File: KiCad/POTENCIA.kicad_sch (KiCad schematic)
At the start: 23 parts, among them J5 Screw_Terminal_01x04, M4 Motor_DC, M5 Motor_DC, M6 Motor_DC, Q2 IRLZ44N, U5 TB6612FNG, U7 ATtiny1616-M, U8 DRV8871DDA

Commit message: cambios en organizacion
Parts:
- removed R27: 10k, Resistor_SMD:R_0805_2012Metric, symbol Device:R
- removed R28, R29: 3.6, Resistor_SMD:R_0805_2012Metric, symbol Device:R
- added R1: 10k, Resistor_SMD:R_0805_2012Metric, symbol Device:R
- added R2, R3: 3.6, Resistor_SMD:R_0805_2012Metric, symbol Device:R
- renumbered C31 to C?, C9 to C?, C33 to C?, C30 to C?, C32 to C?, C34 to C?, D5 to D?, J5 to J?, M5 to M?, M4 to M?, M6 to M?, Q2 to Q?, R24 to R?, R23 to R?, R14 to R?, R1 to R?, R26 to R?, U5 to U?, U7 to U?, U8 to U?
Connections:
- net +3.3V: now also R2.2
- net CALEFACCIÓ: now also R1.1, R3.1
- net GND: now also R1.2
- net T_SEIENTS: now also R2.1
- net at D?.2 (A): now also R3.2
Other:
- moved on the sheet: D?, J?, Q?

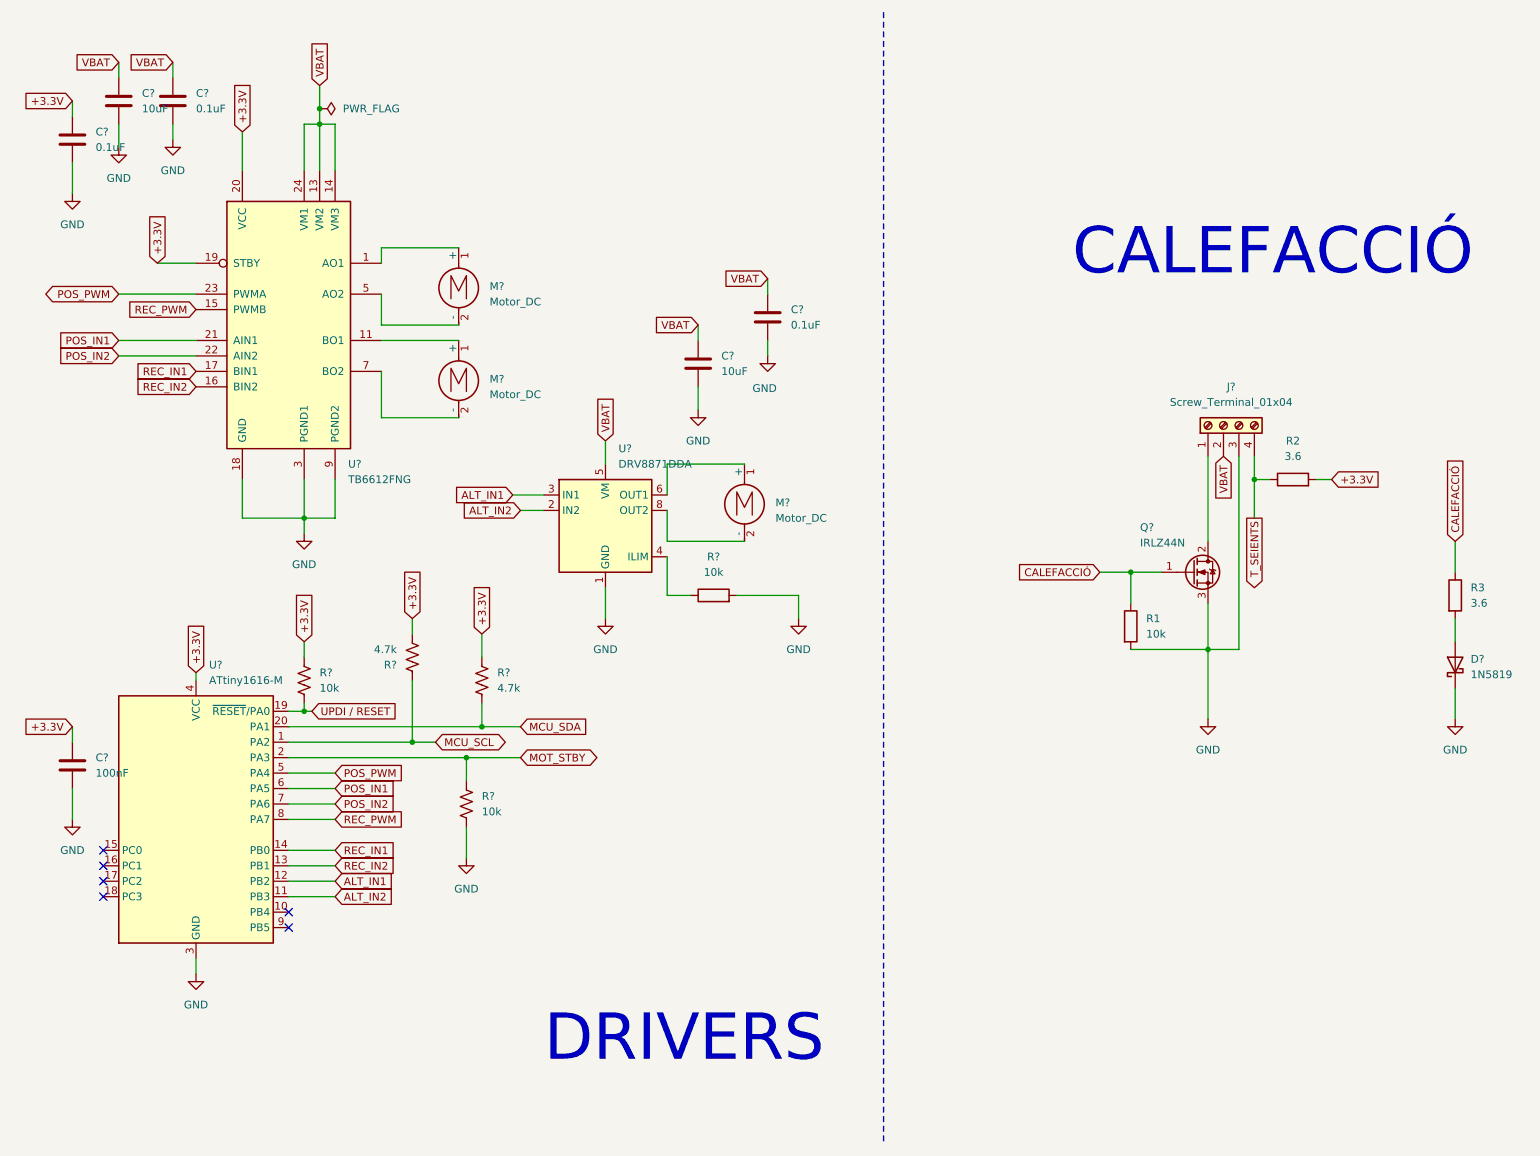
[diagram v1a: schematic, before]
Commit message: Modificació d'errors varis
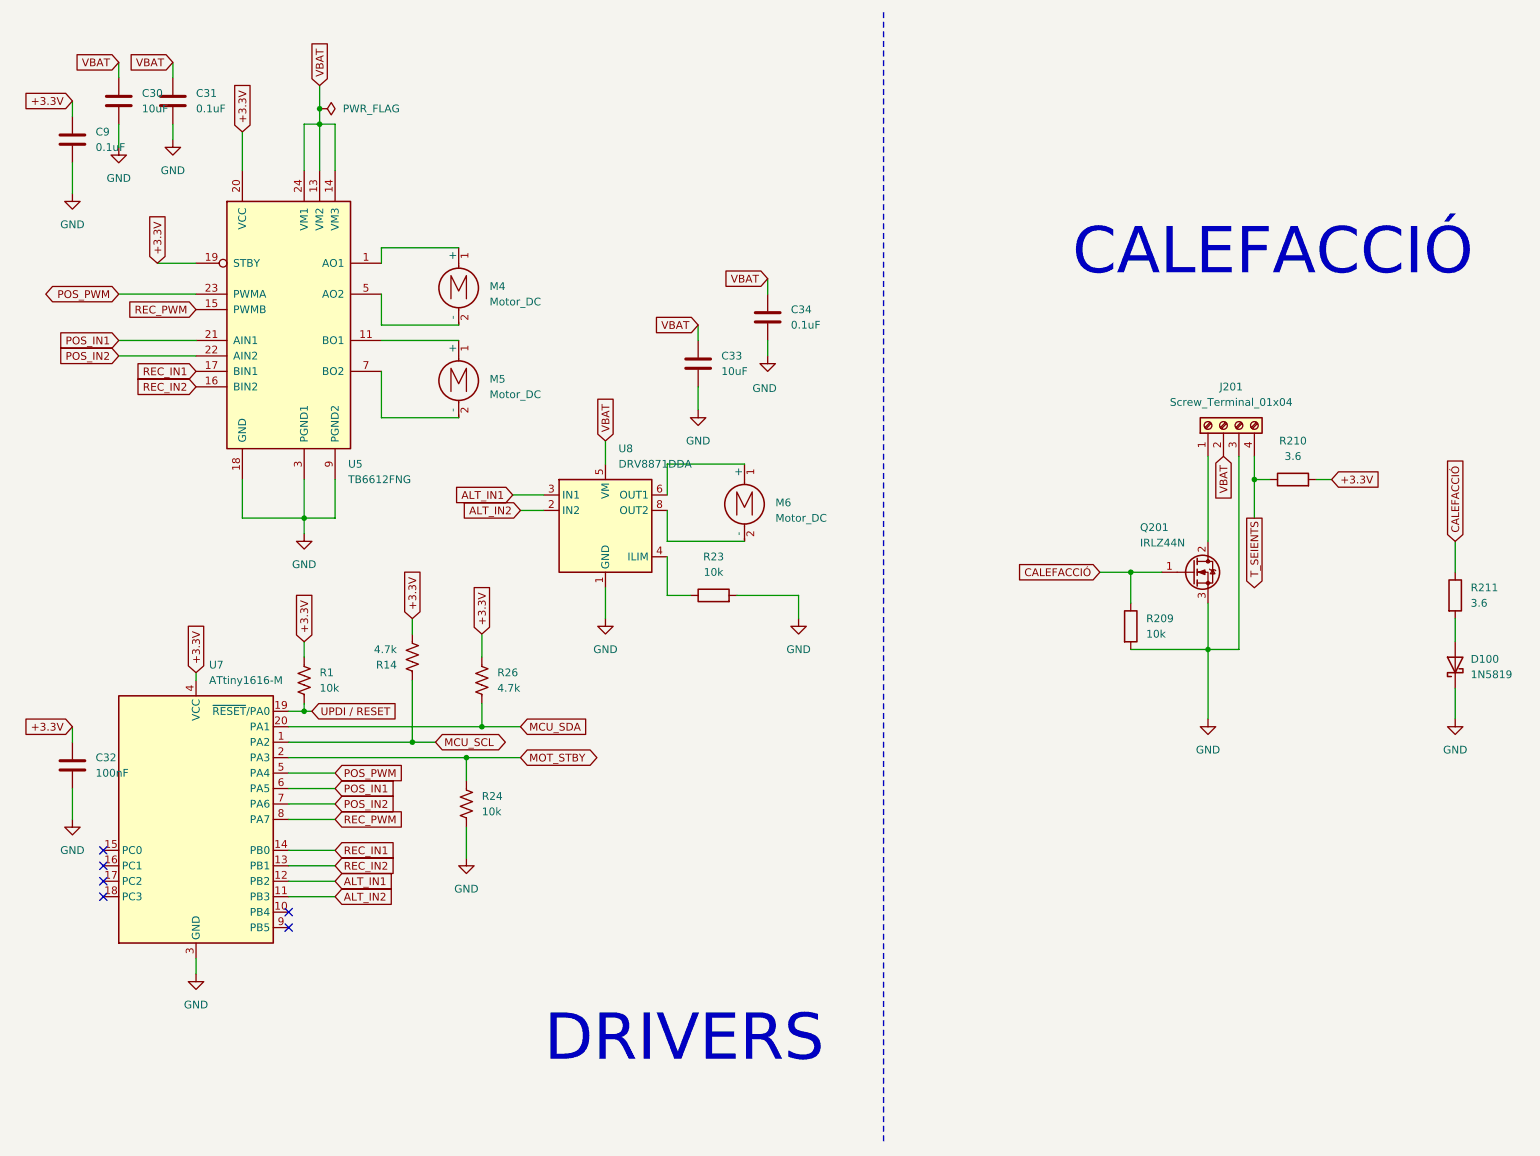
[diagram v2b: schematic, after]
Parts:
- gave numbers to parts that had none: 20
- renumbered R1 to R209, R2 to R210, R3 to R211
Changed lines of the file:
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@@
 	(wire
 		(pts
-			(xy 213.36 85.09) (xy 213.36 99.06)
-		)
-		(stroke
-			(width 0)
-			(type default)
-		)
-	)
-	(wire
-		(pts
 			(xy 40.64 53.34) (xy 46.99 53.34)
 		)
@@
 	(wire
 		(pts
+			(xy 213.36 85.09) (xy 213.36 99.06)
+		)
+		(stroke
+			(width 0)
+			(type default)
+		)
+	)
+	(wire
+		(pts
 			(xy 62.23 134.62) (xy 91.44 134.62)
 		)
@@
 		(dnp no)
 		(fields_autoplaced yes)
-		(property "Reference" "#PWR?"
+		(property "Reference" "#PWR052"
 			(at 129.54 83.82 0)
 			(effects
@@
 		(dnp no)
 		(fields_autoplaced yes)
-		(property "Reference" "R?"
+		(property "Reference" "R24"
 			(at 93.98 140.9699 0)
 			(effects
@@
 		(dnp no)
 		(fields_autoplaced yes)
-		(property "Reference" "#PWR?"
+		(property "Reference" "#PWR048"
 			(at 64.77 104.14 0)
 			(effects
@@
 		(dnp no)
 		(fields_autoplaced yes)
-		(property "Reference" "R?"
+		(property "Reference" "R23"
 			(at 132.08 101.6 90)
 			(effects
@@
 		(on_board yes)
 		(dnp no)
-		(property "Reference" "Q?"
+		(property "Reference" "Q201"
 			(at 202.184 96.774 0)
 			(effects
@@
 				)
 			)
+			(project "SEIENTS_EDD"
+				(path "/b6401b4f-5426-49b8-bb2e-8ecdb19989ef/59990b35-698c-4572-9d1a-e1ee1d49a527"
+					(reference "Q201")
+					(unit 1)
+				)
+			)
 		)
 	)
@@
 		(dnp no)
 		(fields_autoplaced yes)
-		(property "Reference" "U?"
+		(property "Reference" "U5"
 			(at 71.9933 86.36 0)
 			(effects
@@
 		(dnp no)
 		(fields_autoplaced yes)
-		(property "Reference" "#PWR?"
+		(property "Reference" "#PWR055"
 			(at 146.05 118.11 0)
 			(effects
@@
 		(dnp no)
 		(fields_autoplaced yes)
-		(property "Reference" "#PWR02"
+		(property "Reference" "#PWR0106"
 			(at 254 134.62 0)
 			(effects
@@
 				)
 			)
+			(project "SEIENTS_EDD"
+				(path "/b6401b4f-5426-49b8-bb2e-8ecdb19989ef/59990b35-698c-4572-9d1a-e1ee1d49a527"
+					(reference "#PWR0106")
+					(unit 1)
+				)
+			)
 		)
 	)
@@
 		(dnp no)
 		(fields_autoplaced yes)
-		(property "Reference" "U?"
+		(property "Reference" "U7"
 			(at 49.1333 119.38 0)
 			(effects
@@
 		(dnp no)
 		(fields_autoplaced yes)
-		(property "Reference" "C?"
+		(property "Reference" "C31"
 			(at 46.99 25.3999 0)
 			(effects
@@
 		(dnp no)
 		(fields_autoplaced yes)
-		(property "Reference" "#PWR?"
+		(property "Reference" "#PWR053"
 			(at 91.44 157.48 0)
 			(effects
@@
 		(dnp no)
 		(fields_autoplaced yes)
-		(property "Reference" "C?"
+		(property "Reference" "C9"
 			(at 30.48 31.7499 0)
 			(effects
@@
 		(dnp no)
 		(fields_autoplaced yes)
-		(property "Reference" "M?"
+		(property "Reference" "M5"
 			(at 95.25 72.3899 0)
 			(effects
@@
 		(dnp no)
 		(fields_autoplaced yes)
-		(property "Reference" "C?"
+		(property "Reference" "C33"
 			(at 133.35 68.5799 0)
 			(effects
@@
 		(dnp no)
 		(fields_autoplaced yes)
-		(property "Reference" "#PWR?"
+		(property "Reference" "#PWR049"
 			(at 26.67 151.13 0)
 			(effects
@@
 		(dnp no)
 		(fields_autoplaced yes)
-		(property "Reference" "C?"
+		(property "Reference" "C30"
 			(at 38.1 25.3999 0)
 			(effects
@@
 		(dnp no)
 		(fields_autoplaced yes)
-		(property "Reference" "#PWR?"
+		(property "Reference" "#PWR017"
 			(at 26.67 48.26 0)
 			(effects
@@
 		(dnp no)
 		(fields_autoplaced yes)
-		(property "Reference" "#PWR?"
+		(property "Reference" "#PWR020"
 			(at 34.29 40.64 0)
 			(effects
@@
 		(dnp no)
 		(fields_autoplaced yes)
-		(property "Reference" "#FLG?"
+		(property "Reference" "#FLG05"
 			(at 69.215 27.94 0)
 			(effects
@@
 		(on_board yes)
 		(dnp no)
-		(property "Reference" "M?"
+		(property "Reference" "M4"
 			(at 95.25 57.1499 0)
 			(effects
@@
 		(dnp no)
 		(fields_autoplaced yes)
-		(property "Reference" "#PWR01"
+		(property "Reference" "#PWR0102"
 			(at 213.36 134.62 0)
 			(effects
@@
 				)
 			)
+			(project "SEIENTS_EDD"
+				(path "/b6401b4f-5426-49b8-bb2e-8ecdb19989ef/59990b35-698c-4572-9d1a-e1ee1d49a527"
+					(reference "#PWR0102")
+					(unit 1)
+				)
+			)
 		)
 	)
@@
 		(dnp no)
 		(fields_autoplaced yes)
-		(property "Reference" "D?"
+		(property "Reference" "D100"
 			(at 256.54 118.4274 90)
 			(effects
@@
 				)
 			)
+			(project "SEIENTS_EDD"
+				(path "/b6401b4f-5426-49b8-bb2e-8ecdb19989ef/59990b35-698c-4572-9d1a-e1ee1d49a527"
+					(reference "D100")
+					(unit 1)
+				)
+			)
 		)
 	)
@@
 		(dnp no)
 		(fields_autoplaced yes)
-		(property "Reference" "R3"
+		(property "Reference" "R211"
 			(at 256.54 106.6799 0)
 			(effects
@@
 				)
 			)
+			(project "SEIENTS_EDD"
+				(path "/b6401b4f-5426-49b8-bb2e-8ecdb19989ef/59990b35-698c-4572-9d1a-e1ee1d49a527"
+					(reference "R211")
+					(unit 1)
+				)
+			)
 		)
 	)
@@
 		(on_board yes)
 		(dnp no)
-		(property "Reference" "#PWR?"
+		(property "Reference" "#PWR054"
 			(at 140.97 74.93 0)
 			(effects
@@
 		(dnp no)
 		(fields_autoplaced yes)
-		(property "Reference" "J?"
+		(property "Reference" "J201"
 			(at 217.17 73.66 90)
 			(effects
@@
 				)
 			)
+			(project "SEIENTS_EDD"
+				(path "/b6401b4f-5426-49b8-bb2e-8ecdb19989ef/59990b35-698c-4572-9d1a-e1ee1d49a527"
+					(reference "J201")
+					(unit 1)
+				)
+			)
 		)
 	)
@@
 		(dnp no)
 		(fields_autoplaced yes)
-		(property "Reference" "R1"
+		(property "Reference" "R209"
 			(at 203.2 111.7599 0)
 			(effects
@@
 				)
 			)
+			(project "SEIENTS_EDD"
+				(path "/b6401b4f-5426-49b8-bb2e-8ecdb19989ef/59990b35-698c-4572-9d1a-e1ee1d49a527"
+					(reference "R209")
+					(unit 1)
+				)
+			)
 		)
 	)
@@
 		(dnp no)
 		(fields_autoplaced yes)
-		(property "Reference" "U?"
+		(property "Reference" "U8"
 			(at 116.4433 83.82 0)
 			(effects
@@
 		(dnp no)
 		(fields_autoplaced yes)
-		(property "Reference" "C?"
+		(property "Reference" "C32"
 			(at 30.48 134.6199 0)
 			(effects
@@
 		(dnp no)
 		(fields_autoplaced yes)
-		(property "Reference" "#PWR?"
+		(property "Reference" "#PWR050"
 			(at 46.99 176.53 0)
 			(effects
@@
 		(dnp no)
 		(fields_autoplaced yes)
-		(property "Reference" "R?"
+		(property "Reference" "R14"
 			(at 80.01 119.3801 0)
 			(effects
@@
 		(dnp no)
 		(fields_autoplaced yes)
-		(property "Reference" "R?"
+		(property "Reference" "R1"
 			(at 67.31 120.6499 0)
 			(effects
@@
 		(dnp no)
 		(fields_autoplaced yes)
-		(property "Reference" "R?"
+		(property "Reference" "R26"
 			(at 96.52 120.6499 0)
 			(effects
@@
 		(dnp no)
 		(fields_autoplaced yes)
-		(property "Reference" "M?"
+		(property "Reference" "M6"
 			(at 142.24 92.7099 0)
 			(effects
@@
 		(dnp no)
 		(fields_autoplaced yes)
-		(property "Reference" "C?"
+		(property "Reference" "C34"
 			(at 144.78 60.9599 0)
 			(effects
@@
 		(dnp no)
 		(fields_autoplaced yes)
-		(property "Reference" "#PWR?"
+		(property "Reference" "#PWR026"
 			(at 43.18 39.37 0)
 			(effects
@@
 		(dnp no)
 		(fields_autoplaced yes)
-		(property "Reference" "#PWR?"
+		(property "Reference" "#PWR051"
 			(at 114.3 118.11 0)
 			(effects
@@
 		(dnp no)
 		(fields_autoplaced yes)
-		(property "Reference" "R2"
+		(property "Reference" "R210"
 			(at 227.33 82.55 90)
 			(effects
@@
 					(unit 1)
 				)
+			)
+			(project "SEIENTS_EDD"
+				(path "/b6401b4f-5426-49b8-bb2e-8ecdb19989ef/59990b35-698c-4572-9d1a-e1ee1d49a527"
+					(reference "R210")
+					(unit 1)
+				)

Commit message: FootPrints Canviats
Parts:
- M4, M5, M6: footprint Connector_PinHeader_2.54mm:PinHeader_1x02_P2.54mm_Horizontal -> TerminalBlock_Phoenix:TerminalBlock_Phoenix_MKDS-1,5-2-5.08_1x02_P5.08mm_Horizontal
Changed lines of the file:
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@@
 			)
 		)
-		(property "Footprint" "Connector_PinHeader_2.54mm:PinHeader_1x02_P2.54mm_Horizontal"
+		(property "Footprint" "TerminalBlock_Phoenix:TerminalBlock_Phoenix_MKDS-1,5-2-5.08_1x02_P5.08mm_Horizontal"
 			(at 90.17 73.406 0)
 			(effects
@@
 			)
 		)
-		(property "Footprint" "Connector_PinHeader_2.54mm:PinHeader_1x02_P2.54mm_Horizontal"
+		(property "Footprint" "TerminalBlock_Phoenix:TerminalBlock_Phoenix_MKDS-1,5-2-5.08_1x02_P5.08mm_Horizontal"
 			(at 90.17 58.166 0)
 			(effects
@@
 			)
 		)
-		(property "Footprint" "Connector_PinHeader_2.54mm:PinHeader_1x02_P2.54mm_Horizontal"
+		(property "Footprint" "TerminalBlock_Phoenix:TerminalBlock_Phoenix_MKDS-1,5-2-5.08_1x02_P5.08mm_Horizontal"
 			(at 137.16 93.726 0)
 			(effects

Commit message: Rounting
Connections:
- net ALT_IN1: now also U7.16 (PC1); no longer U7.12 (PB2)
- net ALT_IN2: now also U7.15 (PC0); no longer U7.11 (PB3)
- net REC_IN1: now also U7.13 (PB1); no longer U7.14 (PB0)
- net REC_IN2: now also U7.14 (PB0); no longer U7.13 (PB1)
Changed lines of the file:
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@@
 	)
 	(no_connect
-		(at 31.75 152.4)
+		(at 62.23 154.94)
 	)
 	(no_connect
@@
 	)
 	(no_connect
-		(at 31.75 149.86)
-	)
-	(wire
-		(pts
-			(xy 26.67 139.7) (xy 26.67 144.78)
+		(at 62.23 157.48)
+	)
+	(wire
+		(pts
+			(xy 26.67 139.7) (xy 26.67 140.97)
 		)
 		(stroke
@@
 	(wire
 		(pts
-			(xy 62.23 157.48) (xy 69.85 157.48)
-		)
-		(stroke
-			(width 0)
-			(type default)
-		)
-	)
-	(wire
-		(pts
 			(xy 93.98 125.73) (xy 93.98 129.54)
 		)
@@
 		(pts
 			(xy 54.61 88.9) (xy 54.61 95.25)
-		)
-		(stroke
-			(width 0)
-			(type default)
-		)
-	)
-	(wire
-		(pts
-			(xy 62.23 154.94) (xy 69.85 154.94)
 		)
 		(stroke
@@
 	(global_label "REC_IN1"
 		(shape input)
-		(at 69.85 149.86 0)
+		(at 69.85 152.4 0)
 		(fields_autoplaced yes)
 		(effects
@@
 		)
 		(property "Intersheetrefs" "${INTERSHEET_REFS}"
-			(at 80.6366 149.86 0)
+			(at 80.6366 152.4 0)
 			(effects
 				(font
@@
 	(global_label "ALT_IN2"
 		(shape input)
-		(at 69.85 157.48 0)
+		(at 31.75 149.86 180)
+		(fields_autoplaced yes)
+		(effects
+			(font
+				(size 1.27 1.27)
+			)
+			(justify right)
+		)
+		(property "Intersheetrefs" "${INTERSHEET_REFS}"
+			(at 22.2223 149.86 0)
+			(effects
+				(font
+					(size 1.27 1.27)
+				)
+				(justify right)
+				(hide yes)
+			)
+		)
+	)
+	(global_label "VBAT"
+		(shape input)
+		(at 34.29 20.32 180)
+		(fields_autoplaced yes)
+		(effects
+			(font
+				(size 1.27 1.27)
+			)
+			(justify right)
+		)
+		(property "Intersheetrefs" "${INTERSHEET_REFS}"
+			(at 27.5442 20.32 0)
+			(effects
+				(font
+					(size 1.27 1.27)
+				)
+				(justify right)
+				(hide yes)
+			)
+		)
+	)
+	(global_label "POS_IN2"
+		(shape input)
+		(at 69.85 142.24 0)
 		(fields_autoplaced yes)
 		(effects
@@
 		)
 		(property "Intersheetrefs" "${INTERSHEET_REFS}"
-			(at 80.0319 157.48 0)
-			(effects
-				(font
-					(size 1.27 1.27)
-				)
-				(justify left)
-				(hide yes)
-			)
-		)
-	)
-	(global_label "VBAT"
-		(shape input)
-		(at 34.29 20.32 180)
+			(at 80.7576 142.24 0)
+			(effects
+				(font
+					(size 1.27 1.27)
+				)
+				(justify left)
+				(hide yes)
+			)
+		)
+	)
+	(global_label "REC_IN2"
+		(shape input)
+		(at 69.85 149.86 0)
+		(fields_autoplaced yes)
+		(effects
+			(font
+				(size 1.27 1.27)
+			)
+			(justify left)
+		)
+		(property "Intersheetrefs" "${INTERSHEET_REFS}"
+			(at 80.6366 149.86 0)
+			(effects
+				(font
+					(size 1.27 1.27)
+				)
+				(justify left)
+				(hide yes)
+			)
+		)
+	)
+	(global_label "ALT_IN1"
+		(shape input)
+		(at 31.75 152.4 180)
 		(fields_autoplaced yes)
 		(effects
@@
 		)
 		(property "Intersheetrefs" "${INTERSHEET_REFS}"
-			(at 27.5442 20.32 0)
+			(at 22.2223 152.4 0)
 			(effects
 				(font
@@
 				)
 				(justify right)
-				(hide yes)
-			)
-		)
-	)
-	(global_label "POS_IN2"
-		(shape input)
-		(at 69.85 142.24 0)
-		(fields_autoplaced yes)
-		(effects
-			(font
-				(size 1.27 1.27)
-			)
-			(justify left)
-		)
-		(property "Intersheetrefs" "${INTERSHEET_REFS}"
-			(at 80.7576 142.24 0)
-			(effects
-				(font
-					(size 1.27 1.27)
-				)
-				(justify left)
-				(hide yes)
-			)
-		)
-	)
-	(global_label "REC_IN2"
-		(shape input)
-		(at 69.85 152.4 0)
-		(fields_autoplaced yes)
-		(effects
-			(font
-				(size 1.27 1.27)
-			)
-			(justify left)
-		)
-		(property "Intersheetrefs" "${INTERSHEET_REFS}"
-			(at 80.6366 152.4 0)
-			(effects
-				(font
-					(size 1.27 1.27)
-				)
-				(justify left)
-				(hide yes)
-			)
-		)
-	)
-	(global_label "ALT_IN1"
-		(shape input)
-		(at 69.85 154.94 0)
-		(fields_autoplaced yes)
-		(effects
-			(font
-				(size 1.27 1.27)
-			)
-			(justify left)
-		)
-		(property "Intersheetrefs" "${INTERSHEET_REFS}"
-			(at 80.0319 154.94 0)
-			(effects
-				(font
-					(size 1.27 1.27)
-				)
-				(justify left)
 				(hide yes)
 			)
@@
 	(symbol
 		(lib_id "power:GND")
-		(at 26.67 144.78 0)
+		(at 26.67 140.97 0)
 		(unit 1)
 		(exclude_from_sim no)
@@
 		(fields_autoplaced yes)
 		(property "Reference" "#PWR049"
-			(at 26.67 151.13 0)
+			(at 26.67 147.32 0)
 			(effects
 				(font
@@
 		)
 		(property "Value" "GND"
-			(at 26.67 149.86 0)
+			(at 26.67 146.05 0)
 			(effects
 				(font
@@
 		)
 		(property "Footprint" ""
-			(at 26.67 144.78 0)
+			(at 26.67 140.97 0)
 			(effects
 				(font
@@
 		)
 		(property "Datasheet" ""
-			(at 26.67 144.78 0)
+			(at 26.67 140.97 0)
 			(effects
 				(font
@@
 		)
 		(property "Description" "Power symbol creates a global label with name \"GND\" , ground"
-			(at 26.67 144.78 0)
-			(effects
-				(font
+			(at 26.67 140.97 0)
+			(effects
+				(font

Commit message: Modificació als DRIVERS
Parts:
- removed C30, C33: 10uF, Capacitor_THT:CP_Radial_D5.0mm_P2.50mm, symbol Device:C
- removed C31, C34, C9: 0.1uF, Capacitor_SMD:C_0805_2012Metric, symbol Device:C
- added C1, C300, C302: 0.1uF, Capacitor_SMD:C_0805_2012Metric, symbol Device:C
- added C301, C303: 10uF, Capacitor_THT:CP_Radial_D5.0mm_P2.50mm, symbol Device:C
- renumbered C32 to C?, D100 to D?, J201 to J?, M5 to M?, M4 to M?, M6 to M?, Q201 to Q?, R209 to R1, R210 to R2, R211 to R3, R24 to R?, R23 to R?, R14 to R?, R1 to R?, R26 to R?, U5 to U?, U7 to U?, U8 to U?
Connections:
- net +3.3V: now also C300.1, C300.2, C301.1, C301.2
- net VBAT: now also C1.1, C1.2, C302.1, C302.2, C303.1, C303.2
